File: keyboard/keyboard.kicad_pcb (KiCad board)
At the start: 2 copper layers, 214.3 x 140.5 mm, 133 parts, among them SW1 MX_SW_HS, SW10 MX_SW_HS, SW11 MX_SW_HS, SW12 MX_SW_HS, SW13 MX_SW_HS, SW14 MX_SW_HS, SW15 MX_SW_HS, SW16 MX_SW_HS, SW17 MX_SW_HS, SW18 MX_SW_HS, SW19 MX_SW_HS, SW2 MX_SW_HS, SW20 MX_SW_HS, SW21 MX_SW_HS, SW22 MX_SW_HS, SW23 MX_SW_HS, SW24 MX_SW_HS, SW25 MX_SW_HS, SW26 MX_SW_HS, SW27 MX_SW_HS, SW28 MX_SW_HS, SW29 MX_SW_HS, SW3 MX_SW_HS, SW30 MX_SW_HS, SW31 MX_SW_HS, SW32 MX_SW_HS, SW33 MX_SW_HS, SW34 MX_SW_HS, SW35 MX_SW_HS, SW36 MX_SW_HS, SW37 MX_SW_HS, SW38 MX_SW_HS, SW39 MX_SW_HS, SW4 MX_SW_HS, SW40 MX_SW_HS, SW41 MX_SW_HS, SW42 MX_SW_HS, SW43 MX_SW_HS, SW44 MX_SW_HS, SW45 MX_SW_HS, SW46 MX_SW_HS, SW47 MX_SW_HS, SW48 MX_SW_HS, SW49 MX_SW_HS, SW5 MX_SW_HS, SW50 MX_SW_HS, SW51 MX_SW_HS, SW52 MX_SW_HS, SW53 MX_SW_HS, SW54 MX_SW_HS, SW55 MX_SW_HS, SW56 MX_SW_HS, SW57 MX_SW_HS, SW58 MX_SW_HS, SW59 MX_SW_HS, SW6 MX_SW_HS, SW60 MX_SW_HS, SW61 MX_SW_HS, SW62 MX_SW_HS, SW63 MX_SW_HS, SW64 MX_SW_HS, SW7 MX_SW_HS, SW8 MX_SW_HS, SW9 MX_SW_HS, U1 ProMicro

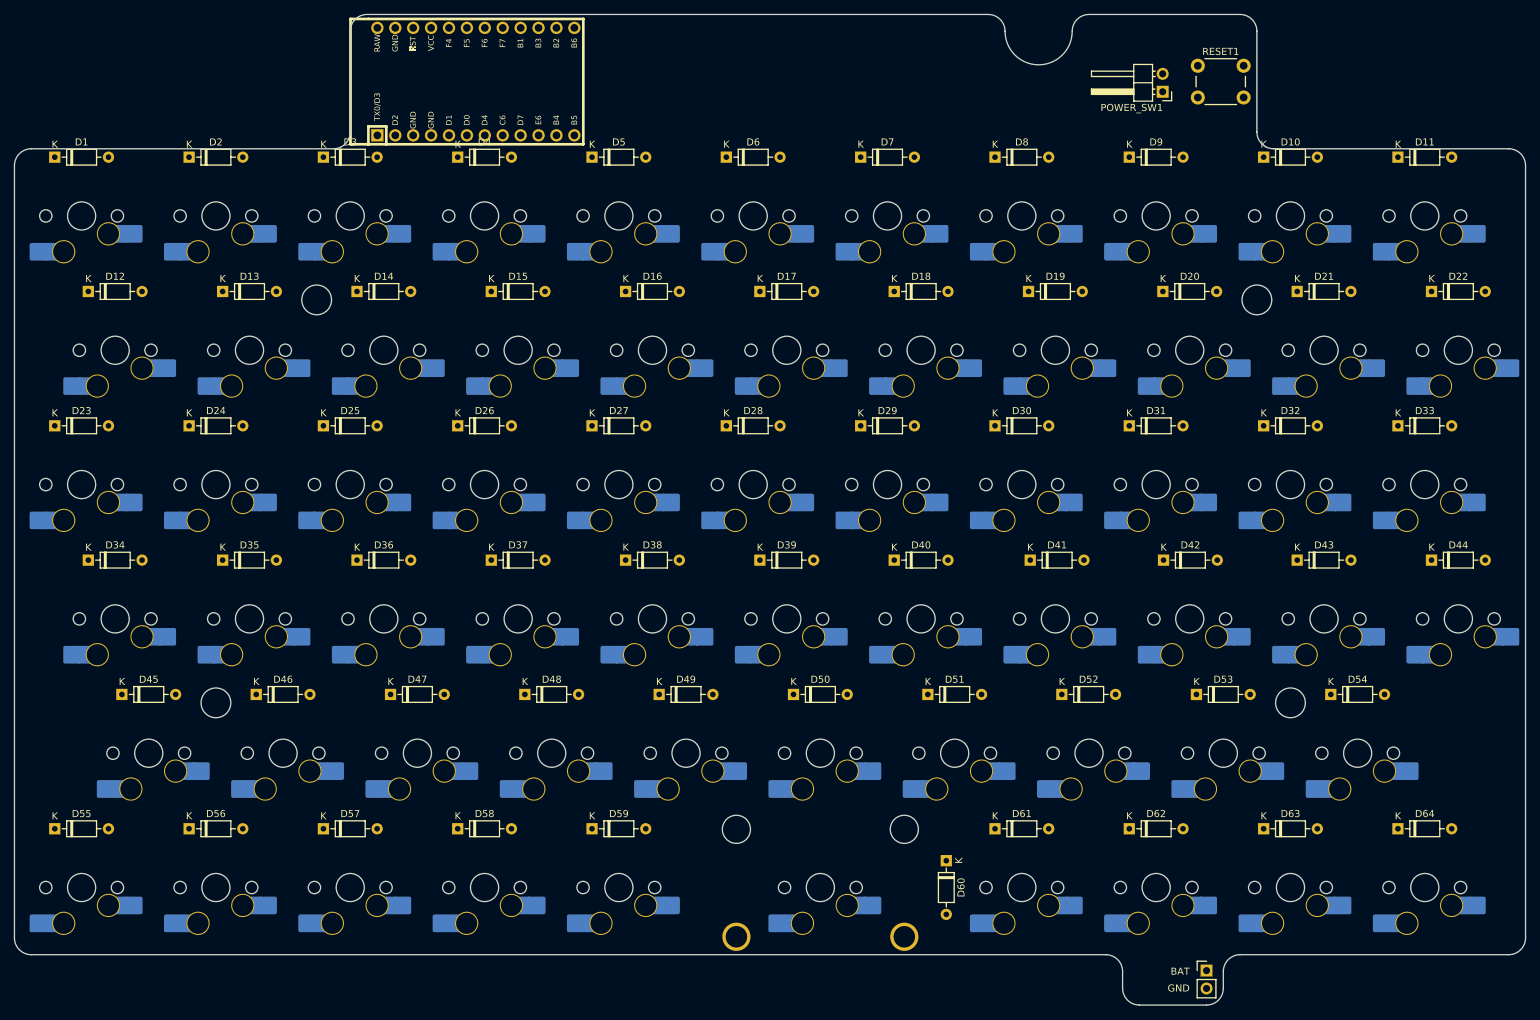
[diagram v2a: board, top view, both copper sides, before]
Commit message: Add the display adapter
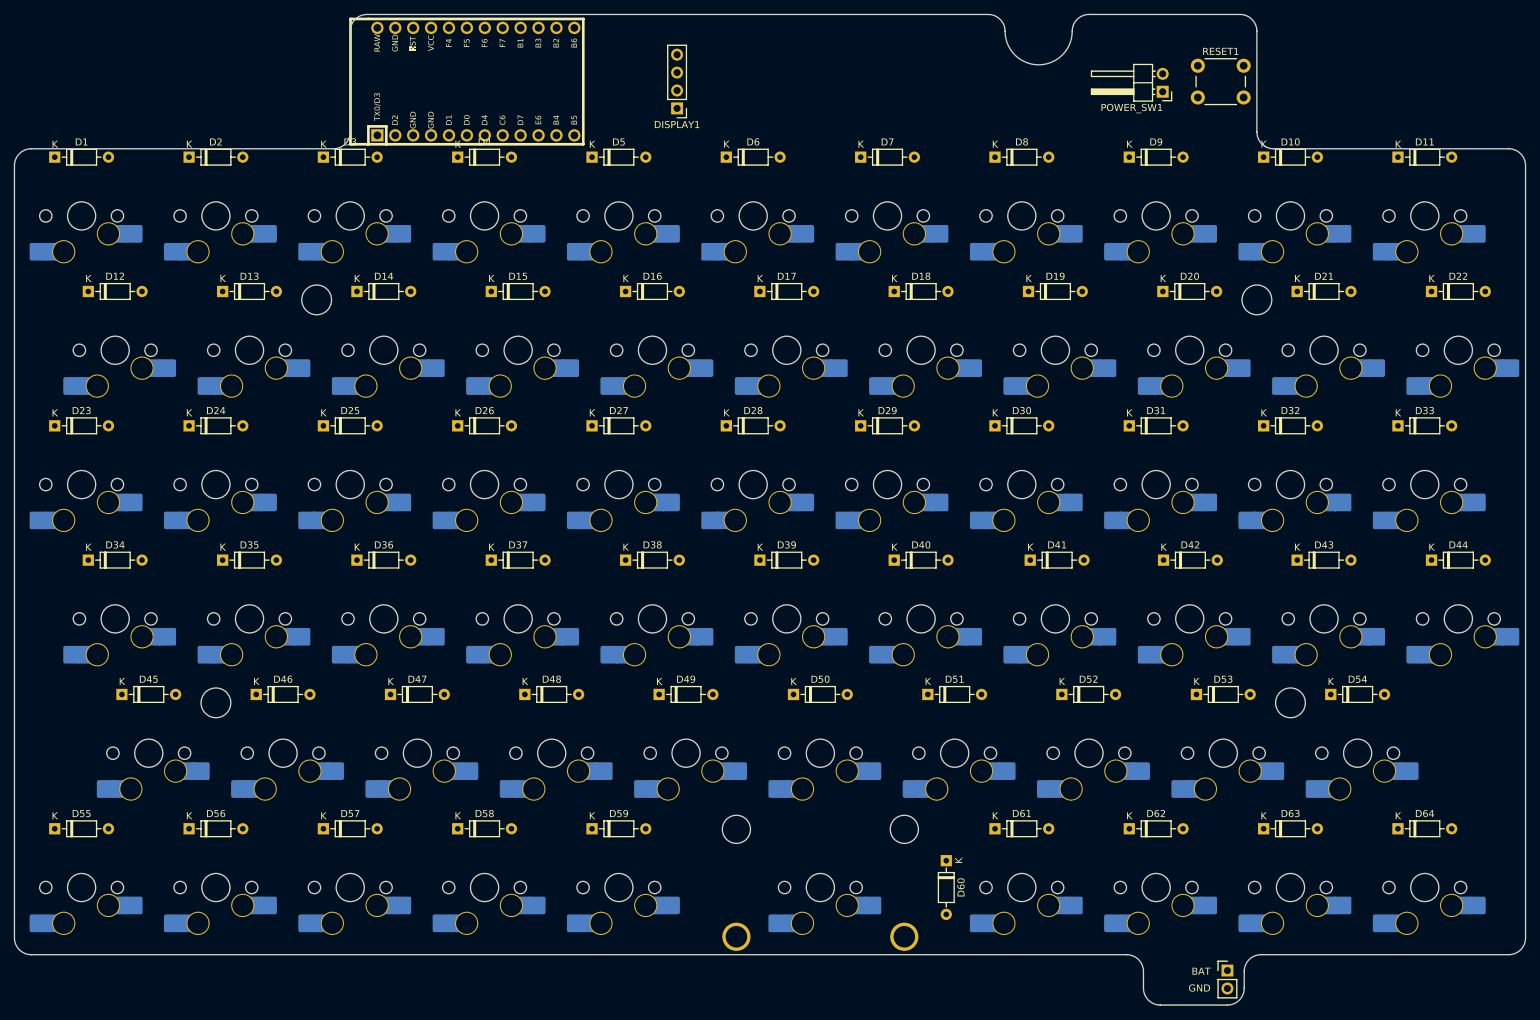
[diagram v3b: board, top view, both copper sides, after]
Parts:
- added DISPLAY1: Conn_01x04_Male, Connector_PinHeader_2.54mm:PinHeader_1x04_P2.54mm_Vertical, F.Cu at (134.5, 27.6)
- moved BATTERY1 2.96 mm to (212.5, 149.9)
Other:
- outline, holes or cut-outs redrawn
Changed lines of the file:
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@@
     )
   )
+  (footprint "Connector_PinHeader_2.54mm:PinHeader_1x04_P2.54mm_Vertical" (layer "F.Cu")
+    (at 134.45775 27.6125 180)
+    (descr "Through hole straight pin header, 1x04, 2.54mm pitch, single row")
+    (tags "Through hole pin header THT 1x04 2.54mm single row")
+    (property "Sheetfile" "keyboard.kicad_sch")
+    (property "Sheetname" "")
+    (attr through_hole)
+    (fp_text reference "DISPLAY1" (at 0 -2.33) (layer "F.SilkS")
+      (effects (font (size 1 1) (thickness 0.15)))
+    )
+    (fp_text value "Conn_01x04_Male" (at 0 9.95) (layer "F.Fab")
+      (effects (font (size 1 1) (thickness 0.15)))
+    )
+    (fp_text user "${REFERENCE}" (at 0 3.81 90) (layer "F.Fab")
+      (effects (font (size 1 1) (thickness 0.15)))
+    )
+    (fp_line (start -1.33 0) (end -1.33 -1.33) (layer "F.SilkS") (width 0.12))
+    (fp_line (start -1.33 1.27) (end -1.33 8.95) (layer "F.SilkS") (width 0.12))
+    (fp_line (start -1.33 8.95) (end 1.33 8.95) (layer "F.SilkS") (width 0.12))
+    (fp_line (start -1.33 -1.33) (end 0 -1.33) (layer "F.SilkS") (width 0.12))
+    (fp_line (start -1.33 1.27) (end 1.33 1.27) (layer "F.SilkS") (width 0.12))
+    (fp_line (start 1.33 1.27) (end 1.33 8.95) (layer "F.SilkS") (width 0.12))
+    (fp_line (start 1.8 9.4) (end 1.8 -1.8) (layer "F.CrtYd") (width 0.05))
+    (fp_line (start -1.8 -1.8) (end -1.8 9.4) (layer "F.CrtYd") (width 0.05))
+    (fp_line (start 1.8 -1.8) (end -1.8 -1.8) (layer "F.CrtYd") (width 0.05))
+    (fp_line (start -1.8 9.4) (end 1.8 9.4) (layer "F.CrtYd") (width 0.05))
+    (fp_line (start -0.635 -1.27) (end 1.27 -1.27) (layer "F.Fab") (width 0.1))
+    (fp_line (start -1.27 -0.635) (end -0.635 -1.27) (layer "F.Fab") (width 0.1))
+    (fp_line (start -1.27 8.89) (end -1.27 -0.635) (layer "F.Fab") (width 0.1))
+    (fp_line (start 1.27 8.89) (end -1.27 8.89) (layer "F.Fab") (width 0.1))
+    (fp_line (start 1.27 -1.27) (end 1.27 8.89) (layer "F.Fab") (width 0.1))
+    (pad "1" thru_hole rect (at 0 0 180) (size 1.7 1.7) (drill 1) (layers *.Cu *.Mask)
+      (net 81 "GND") (pinfunction "Pin_1") (pintype "passive"))
+    (pad "2" thru_hole oval (at 0 2.54 180) (size 1.7 1.7) (drill 1) (layers *.Cu *.Mask)
+      (net 85 "VCC") (pinfunction "Pin_2") (pintype "passive"))
+    (pad "3" thru_hole oval (at 0 5.08 180) (size 1.7 1.7) (drill 1) (layers *.Cu *.Mask)
+      (net 84 "SCL") (pinfunction "Pin_3") (pintype "passive"))
+    (pad "4" thru_hole oval (at 0 7.62 180) (size 1.7 1.7) (drill 1) (layers *.Cu *.Mask)
+      (net 83 "SDA") (pinfunction "Pin_4") (pintype "passive"))
+    (model "${KICAD6_3DMODEL_DIR}/Connector_PinHeader_2.54mm.3dshapes/PinHeader_1x04_P2.54mm_Vertical.wrl"
+      (offset (xyz 0 0 0))
+      (scale (xyz 1 1 1))
+      (rotate (xyz 0 0 0))
+    )
+  )
   (footprint "Diode_THT:D_DO-35_SOD27_P7.62mm_Horizontal" (layer "F.Cu")
     (at 141.44625 34.528125)
@@
   )
   (footprint "Connector_PinHeader_2.54mm:PinHeader_1x02_P2.54mm_Vertical" (layer "F.Cu")
-    (at 209.55 149.89)
+    (at 212.5125 149.89)
     (descr "Through hole straight pin header, 1x02, 2.54mm pitch, single row")
     (tags "Through hole pin header THT 1x02 2.54mm single row")
@@
   (gr_line (start 216.69375 30.95625) (end 216.69375 16.66875) (layer "Edge.Cuts") (width 0.1))
   (gr_circle (center 221.45625 111.91875) (end 223.56625 111.91875) (layer "Edge.Cuts") (width 0.1) (fill none))
-  (gr_line (start 252.4125 147.6375) (end 214.3125 147.6375) (layer "Edge.Cuts") (width 0.1))
-  (gr_arc (start 211.93125 150.01875) (mid 212.628702 148.334952) (end 214.3125 147.6375) (layer "Edge.Cuts") (width 0.1))
+  (gr_line (start 252.4125 147.6375) (end 217.275 147.6375) (layer "Edge.Cuts") (width 0.1))
+  (gr_arc (start 214.89375 150.01875) (mid 215.59122 148.334984) (end 217.275 147.6375) (layer "Edge.Cuts") (width 0.1))
   (gr_line (start 254.79375 145.25625) (end 254.79375 35.71875) (layer "Edge.Cuts") (width 0.1))
-  (gr_line (start 209.55 154.78125) (end 200.025 154.78125) (layer "Edge.Cuts") (width 0.1))
+  (gr_line (start 212.5125 154.78125) (end 202.9875 154.78125) (layer "Edge.Cuts") (width 0.1))
   (gr_arc (start 190.5 16.66875) (mid 191.197452 14.984952) (end 192.88125 14.2875) (layer "Edge.Cuts") (width 0.1))
   (gr_arc (start 252.4125 33.3375) (mid 254.096269 34.034981) (end 254.79375 35.71875) (layer "Edge.Cuts") (width 0.1))
   (gr_arc (start 178.59375 14.2875) (mid 180.277548 14.984952) (end 180.975 16.66875) (layer "Edge.Cuts") (width 0.1))
   (gr_circle (center 69.05625 111.91875) (end 71.16625 111.91875) (layer "Edge.Cuts") (width 0.1) (fill none))
-  (gr_line (start 42.8625 147.6375) (end 195.2625 147.6375) (layer "Edge.Cuts") (width 0.1))
-  (gr_arc (start 211.93125 152.4) (mid 211.233798 154.083798) (end 209.55 154.78125) (layer "Edge.Cuts") (width 0.1))
+  (gr_line (start 42.8625 147.6375) (end 198.225 147.6375) (layer "Edge.Cuts") (width 0.1))
+  (gr_arc (start 214.89375 152.4) (mid 214.196298 154.083798) (end 212.5125 154.78125) (layer "Edge.Cuts") (width 0.1))
   (gr_arc (start 254.79375 145.25625) (mid 254.096269 146.940019) (end 252.4125 147.6375) (layer "Edge.Cuts") (width 0.1))
   (gr_arc (start 40.48125 35.71875) (mid 41.178717 34.034967) (end 42.8625 33.3375) (layer "Edge.Cuts") (width 0.1))
@@
   (gr_line (start 85.725 33.3375) (end 42.8625 33.3375) (layer "Edge.Cuts") (width 0.1))
   (gr_arc (start 214.3125 14.2875) (mid 215.996298 14.984952) (end 216.69375 16.66875) (layer "Edge.Cuts") (width 0.1))
-  (gr_arc (start 200.025 154.78125) (mid 198.341202 154.083798) (end 197.64375 152.4) (layer "Edge.Cuts") (width 0.1))
-  (gr_line (start 197.64375 152.4) (end 197.64375 150.01875) (layer "Edge.Cuts") (width 0.1))
+  (gr_arc (start 202.9875 154.78125) (mid 201.303702 154.083798) (end 200.60625 152.4) (layer "Edge.Cuts") (width 0.1))
+  (gr_line (start 200.60625 152.4) (end 200.60625 150.01875) (layer "Edge.Cuts") (width 0.1))
   (gr_arc (start 190.5 16.66875) (mid 185.7375 21.43125) (end 180.975 16.66875) (layer "Edge.Cuts") (width 0.1))
   (gr_arc (start 42.8625 147.6375) (mid 41.178731 146.940019) (end 40.48125 145.25625) (layer "Edge.Cuts") (width 0.1))
-  (gr_arc (start 195.2625 147.6375) (mid 196.946298 148.334952) (end 197.64375 150.01875) (layer "Edge.Cuts") (width 0.1))
-  (gr_line (start 211.93125 150.01875) (end 211.93125 152.4) (layer "Edge.Cuts") (width 0.1))
+  (gr_arc (start 198.225 147.6375) (mid 199.908816 148.334949) (end 200.60625 150.01875) (layer "Edge.Cuts") (width 0.1))
+  (gr_line (start 214.89375 150.01875) (end 214.89375 152.4) (layer "Edge.Cuts") (width 0.1))
   (gr_line (start 192.88125 14.2875) (end 214.3125 14.2875) (layer "Edge.Cuts") (width 0.1))
   (gr_arc (start 219.075 33.3375) (mid 217.391202 32.640048) (end 216.69375 30.95625) (layer "Edge.Cuts") (width 0.1))
   (gr_line (start 219.075 33.3375) (end 252.4125 33.3375) (layer "Edge.Cuts") (width 0.1))
-  (gr_text "GND" (at 207.16875 152.4) (layer "F.SilkS")
+  (gr_text "GND" (at 210.13125 152.4) (layer "F.SilkS")
     (effects (font (size 1 1) (thickness 0.15)) (justify right))
   )
-  (gr_text "BAT" (at 207.16875 150.01875) (layer "F.SilkS")
+  (gr_text "BAT" (at 210.13125 150.01875) (layer "F.SilkS")
     (effects (font (size 1 1) (thickness 0.15)) (justify right))
   )

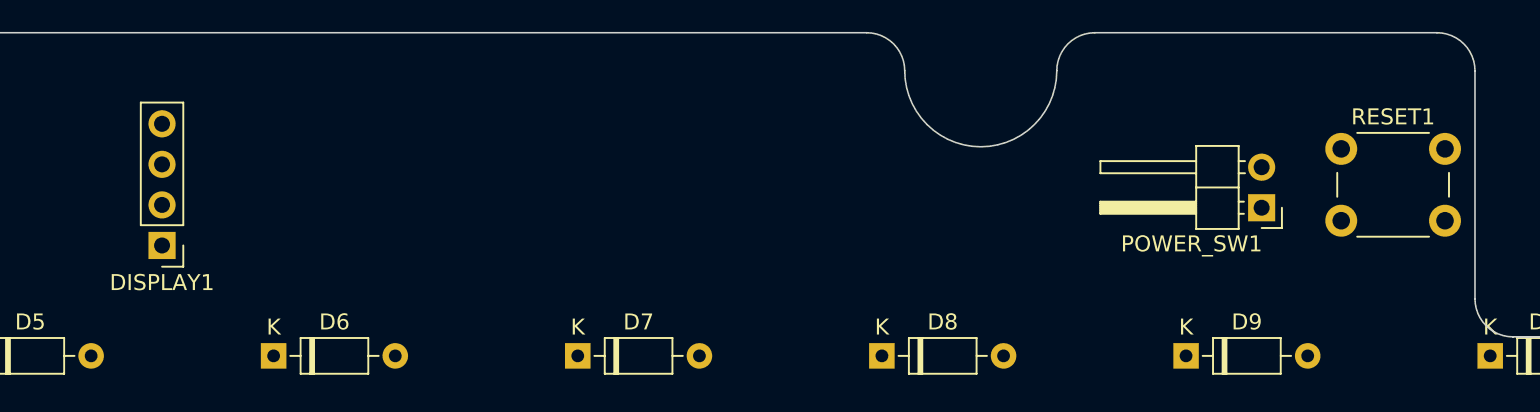
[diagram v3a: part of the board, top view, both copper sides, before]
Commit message: Clean up the silkscreen a little
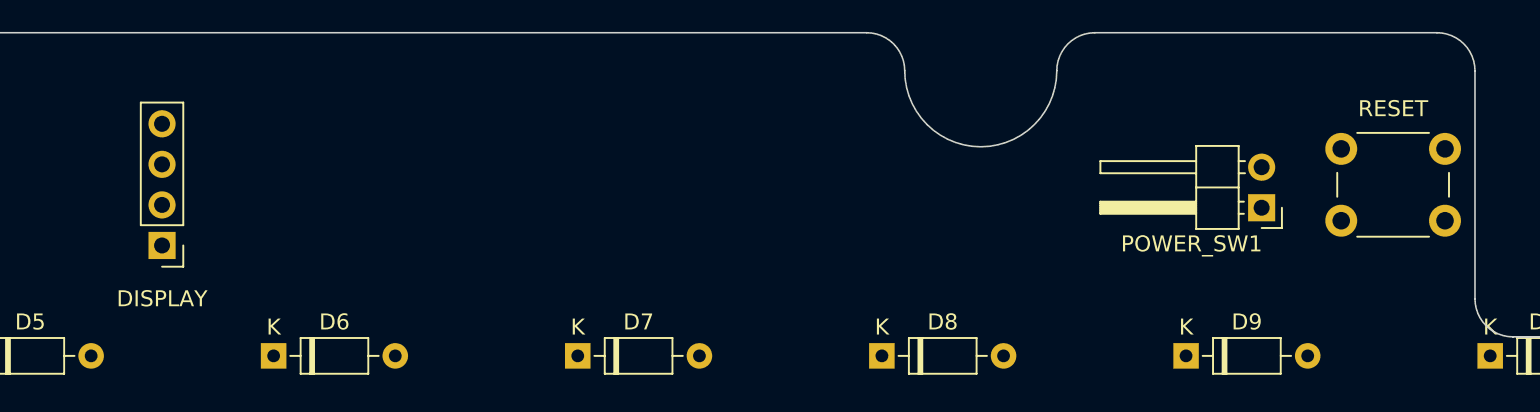
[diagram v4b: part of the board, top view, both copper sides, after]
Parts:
- renumbered DISPLAY1 to DISPLAY, RESET1 to RESET
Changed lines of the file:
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@@
     (property "Sheetname" "")
     (attr through_hole)
-    (fp_text reference "DISPLAY1" (at 0 -2.33) (layer "F.SilkS")
+    (fp_text reference "DISPLAY" (at 0 -3.34375) (layer "F.SilkS")
       (effects (font (size 1 1) (thickness 0.15)))
     )
-    (fp_text value "Conn_01x04_Male" (at 0 9.95) (layer "F.Fab")
+    (fp_text value "Conn_01x04_Male" (at 0 9.95) (layer "F.Fab") hide
       (effects (font (size 1 1) (thickness 0.15)))
     )
@@
       (effects (font (size 1 1) (thickness 0.15)))
     )
-    (fp_text value "Conn_01x02_Male" (at 4.385 4.81) (layer "F.Fab")
+    (fp_text value "Conn_01x02_Male" (at 4.385 4.81) (layer "F.Fab") hide
       (effects (font (size 1 1) (thickness 0.15)))
     )
-    (fp_text user "${REFERENCE}" (at 2.77 1.27 90) (layer "F.Fab")
+    (fp_text user "${REFERENCE}" (at 2.77 1.27 90) (layer "F.Fab") hide
       (effects (font (size 1 1) (thickness 0.15)))
     )
@@
     (property "Sheetname" "")
     (attr through_hole)
-    (fp_text reference "RESET1" (at 3.25 -2) (layer "F.SilkS")
+    (fp_text reference "RESET" (at 3.25 -2.5125) (layer "F.SilkS")
       (effects (font (size 1 1) (thickness 0.15)))
     )
